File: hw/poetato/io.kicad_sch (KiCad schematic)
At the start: 41 parts, among them J1 1757349, J2 1757268, Q6 NTK3134N, T1 1308_750319693, U15 SN6507DGQR, U19 TPS26625DRCR

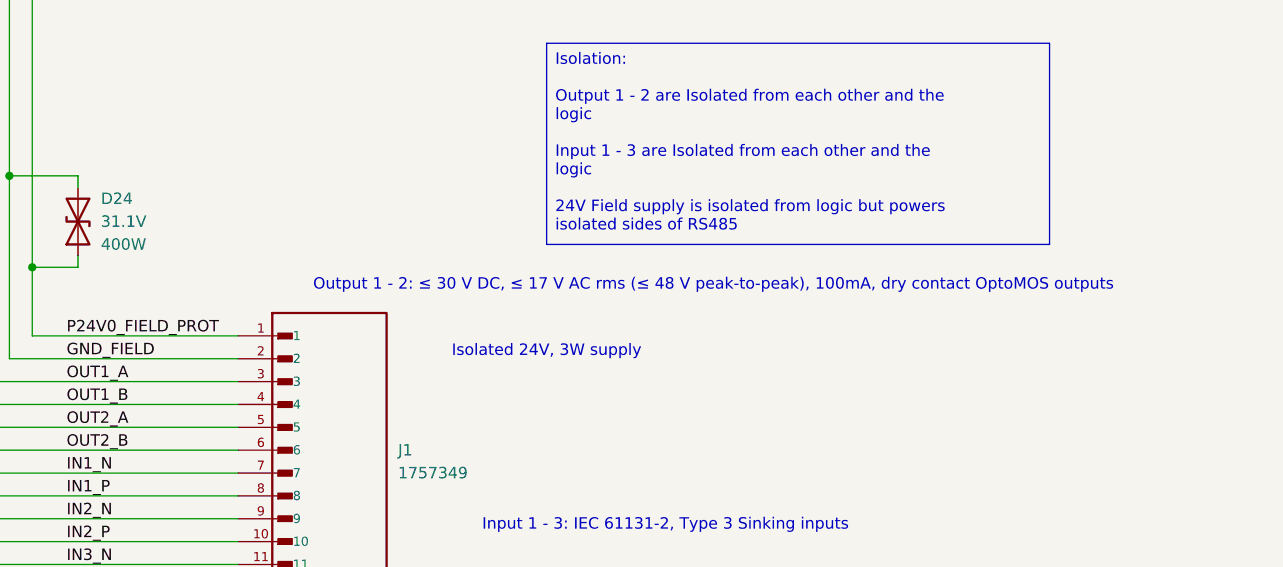
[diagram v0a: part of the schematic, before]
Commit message: hw: RS485_RXD pull-up, 3V3 buck EN threshold, DC-only output rating
- R8 100 kOhm pull-up from RS485_RXD to P3V3 (review X3-1)
- 3V3 buck EN divider R23 127 kOhm / R87 20.5 kOhm (replaces R86
  47 kOhm): on at ~8.6 V, off at ~7.2 V (review Q-4)
- IO sheet note: outputs rated <= 30 V DC only (review E1-1)

Co-Authored-By: Claude Opus 5.5 <noreply@anthropic.com>
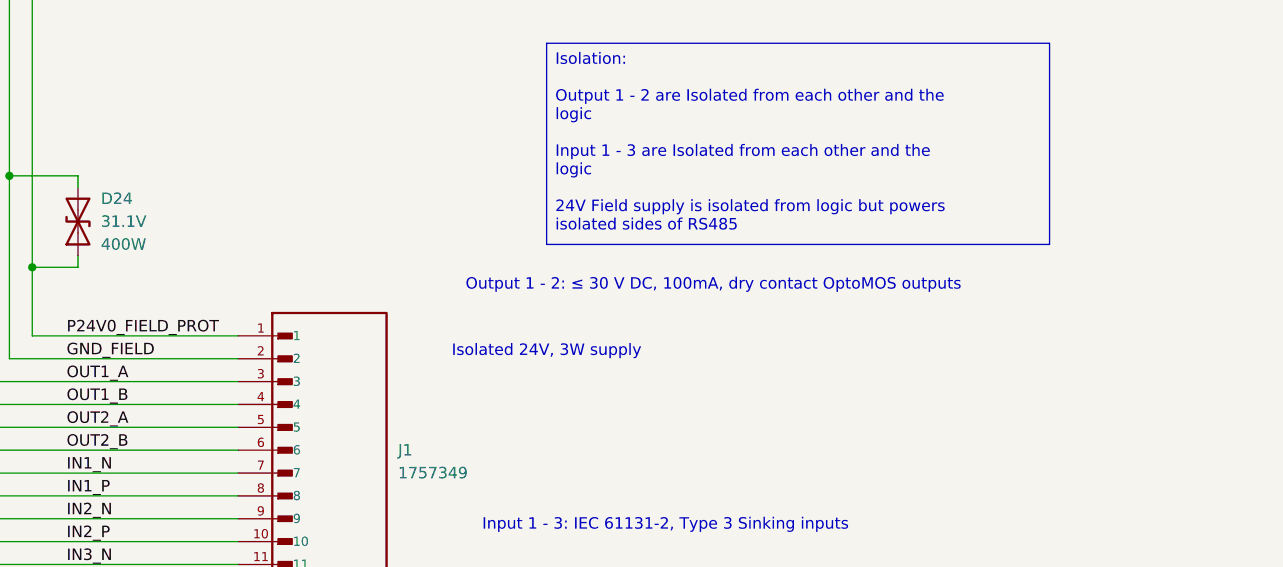
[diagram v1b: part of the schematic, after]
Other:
- note added: "Output 1 - 2: ≤ 30 V DC, 100mA, dry contact OptoMOS outputs"
- note removed: "Output 1 - 2: ≤ 30 V DC, ≤ 17 V AC rms (≤ 48 V peak-to-peak), 100mA, dry contact OptoMOS outputs"
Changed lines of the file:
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@@
 		)
 	)
-	(text "Output 1 - 2: ≤ 30 V DC, ≤ 17 V AC rms (≤ 48 V peak-to-peak), 100mA, dry contact OptoMOS outputs"
+	(text "Output 1 - 2: ≤ 30 V DC, 100mA, dry contact OptoMOS outputs"
 		(exclude_from_sim no)
 		(at 352.552 140.462 0)
